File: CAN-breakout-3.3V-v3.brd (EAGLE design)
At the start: 27.9 x 15.2 mm, 11 parts, among them IC1 TJA1049

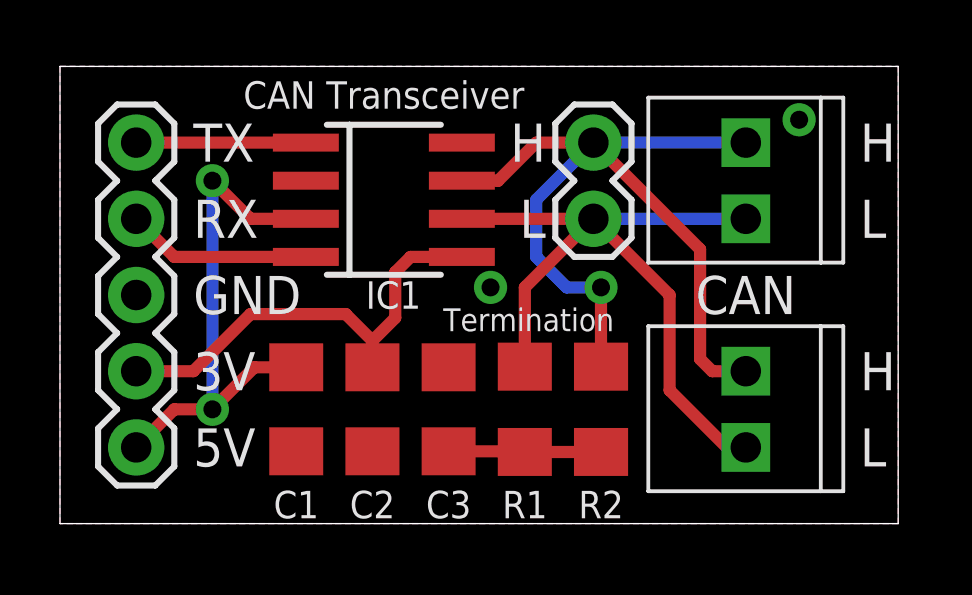
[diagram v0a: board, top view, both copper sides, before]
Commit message: Add 3.3V variant
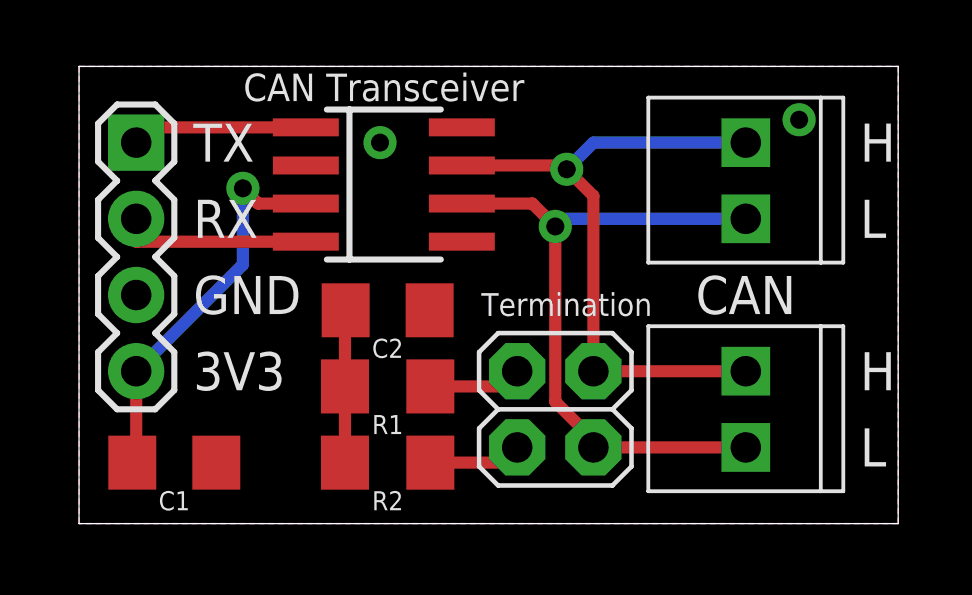
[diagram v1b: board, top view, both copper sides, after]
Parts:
- removed C3: 0.01u, rcl:C1206
- C2: value 0.1u -> 0.01u
- IC1: value TJA1049 -> SN65HVD232
- JP1: device SparkFun-Connectors:1X05 -> SparkFun-Connectors:1X04
- JP2: device SparkFun-Connectors:1X02 -> CAN:2X2
- moved R2 7.33 mm to (10.9, 2.03), turned to 0 degrees
- moved JP2 5.68 mm to (15.2, 5.08), turned to 270 degrees
- moved R1 4.64 mm to (10.9, 4.57), turned to 0 degrees
- moved C1 4.44 mm to (3.81, 2.03), turned to 180 degrees
- moved C2 3.34 mm to (10.9, 7.11), turned to 180 degrees
- moved U$3 3.24 mm to (6.55, 4.11), turned to 270 degrees
- moved IC1 0.51 mm to (10.8, 11.3)
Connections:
- removed net 5V: C1.2, IC1.3, JP1.5
- new net N$1: JP2.1, R1.2
- new net N$10: JP2.3, R2.2
- net 3.3V: now also C1.2, IC1.3; no longer C2.2, IC1.5
- net CANH: no longer R2.2
- net CANL: now also JP2.4; no longer JP2.1, R1.2
- net GND: no longer C3.1, IC1.8
- net N$7: now also C2.2; no longer C3.2
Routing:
- net 5V: track 17.7 -> 0.00 mm, vias 2 -> 0
- net CANH: track 30.2 -> 22.5 mm
- net N$10: track 0.00 -> 3.11 mm
- net N$1: track 0.00 -> 3.11 mm
- net CANL: track 25.4 -> 22.9 mm, vias 0 -> 1
- net 3.3V: track 15.1 -> 13.0 mm, vias 0 -> 1
- net CANTX: track 5.66 -> 6.16 mm
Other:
- board size 27.9 x 15.2 mm -> 27.3 x 15.2 mm
- board text added: "3V3"
- board text added: "Close jumper at both ends of bus for termination"
- board text added: "Particle pins RX=D2 TX=D1"
- board text added: "Screw terminals are the same bus"
- board text added: "V3"
- board text removed: "3V"
- board text removed: "5V"
- board text removed: "Particle wiring: RX=D2, TX=D1, 3V=3V3, 5V=VIN, GND=GND"
- board text removed: "Screw terminals are the same bus Solder R1=R2=62 at ends of bus"
- board text removed: "V2"
